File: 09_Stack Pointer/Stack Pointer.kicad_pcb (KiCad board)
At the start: 2 copper layers, 100 x 100 mm, 49 parts, among them J1 Data bus, J2 Address bus 1, J3 Address bus 2, J4 Input 1, U1 74LS191, U2 74LS02, U3 74LS139, U4 74LS191, U5 74LS191, U6 74LS245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

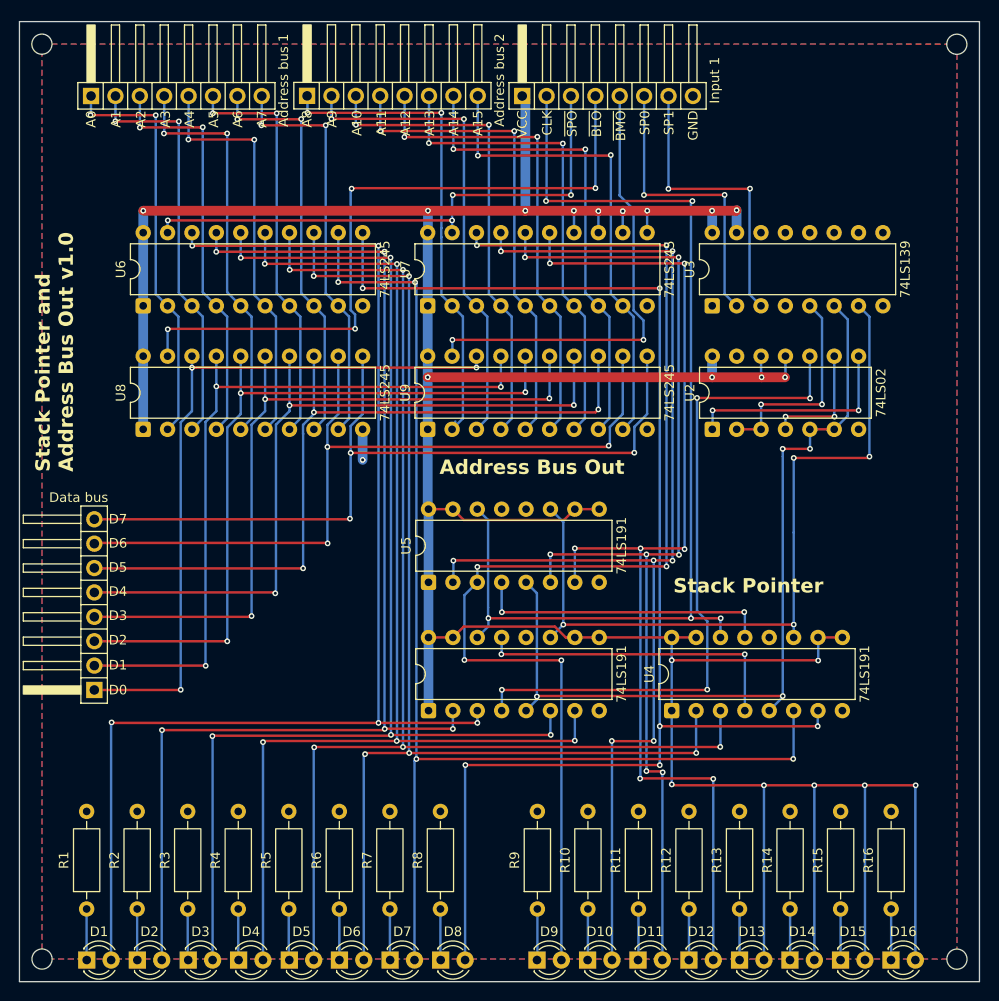
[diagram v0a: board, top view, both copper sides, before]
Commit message: Last revision of the cpu, all boards have been ordered. Implementation to be tested and documented in following commits.
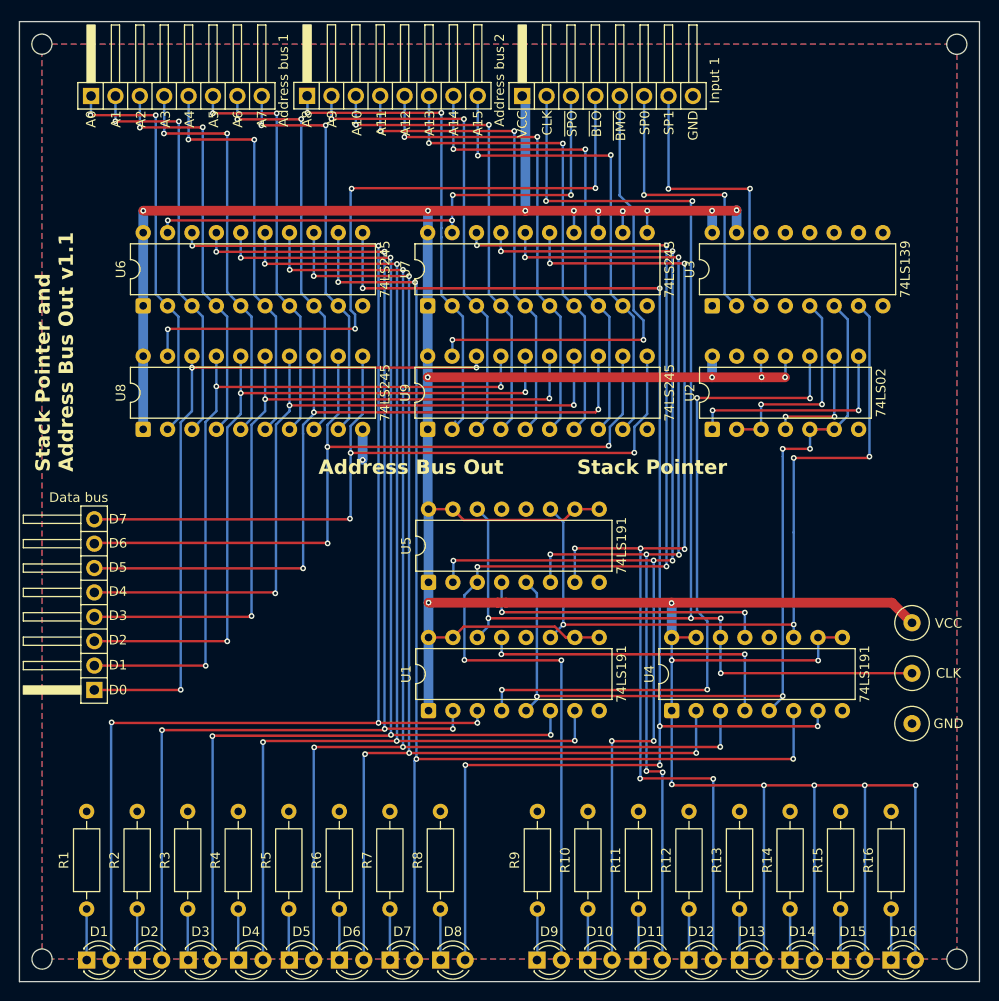
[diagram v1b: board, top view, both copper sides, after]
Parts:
- added TP1: VCC, TestPoint:TestPoint_Loop_D3.50mm_Drill0.9mm_Beaded, F.Cu at (143.0, 105.6)
- added TP2: CLK, TestPoint:TestPoint_Loop_D3.50mm_Drill0.9mm_Beaded, F.Cu at (143.0, 110.9)
- added TP3: GND, TestPoint:TestPoint_Loop_D3.50mm_Drill0.9mm_Beaded, F.Cu at (143.0, 116.1)
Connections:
- net SP0 renamed SC0
- net SP1 renamed SC1
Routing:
- net VCC: track 387.5 -> 434.8 mm, vias 20 -> 22
- net CLK: track 110.3 -> 133.9 mm, vias 5 -> 6
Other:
- board text added: "Stack Pointer and Address Bus Out v1.1"
- board text removed: "Stack Pointer and Address Bus Out v1.0"
